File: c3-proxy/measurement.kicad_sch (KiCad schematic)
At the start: 31 parts, among them Q8 DMP2035UQ-7, SW2 SW_DP3T, U1 MCP2221AxST, U5 TS5A21366, U6 MAX892LEUA+T, U7 MIC23050-SYML, U8 LTC4412xS6

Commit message: layout cleanup, add bypass to U1-Vdd
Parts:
- added C10: 100n, oresat-passives:0603-C-NOSILK, symbol Device:C_Small
- D1, D2, D3, D4: footprint oresat-passives:0603-C-NOSILK -> LED_SMD:LED_0603_1608Metric
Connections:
- net 3.3V: now also C10.2
- net GND: now also C10.1
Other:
- note added: "Bypass for pin 1"

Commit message: polishing, adding 3D paths
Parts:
- C10: DPN 490-GRT188R71E105KE13DCT-ND -> 399-6856-1-ND; MFR Murata Electronics -> KEMET; MPN GRT188R71E105KE13D -> C0603C104K5RACAUTO
- R13, R14: DPN RMCF0603FT10K0CT-ND -> RMCF0603FT4K70CT-ND; MPN RMCF0603FT10K0 -> RMCF0603FT4K70
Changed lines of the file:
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@@
 			)
 		)
-		(property "Description" "10 kOhms ±1% 0.1W, 1/10W Chip Resistor 0603 (1608 Metric) Automotive AEC-Q200 Thick Film"
+		(property "Description" "4.7 kOhms ±1% 0.1W, 1/10W Chip Resistor 0603 (1608 Metric) Automotive AEC-Q200 Thick Film"
 			(at 181.61 140.97 0)
 			(hide yes)
@@
 			)
 		)
-		(property "DPN" "RMCF0603FT10K0CT-ND"
+		(property "DPN" "RMCF0603FT4K70CT-ND"
 			(at 181.61 140.97 0)
 			(hide yes)
@@
 			)
 		)
-		(property "MPN" "RMCF0603FT10K0"
+		(property "MPN" "RMCF0603FT4K70"
 			(at 181.61 140.97 0)
 			(hide yes)
@@
 			)
 		)
-		(property "Description" "10 kOhms ±1% 0.1W, 1/10W Chip Resistor 0603 (1608 Metric) Automotive AEC-Q200 Thick Film"
+		(property "Description" "4.7 kOhms ±1% 0.1W, 1/10W Chip Resistor 0603 (1608 Metric) Automotive AEC-Q200 Thick Film"
 			(at 186.69 140.97 0)
 			(hide yes)
@@
 			)
 		)
-		(property "DPN" "RMCF0603FT10K0CT-ND"
+		(property "DPN" "RMCF0603FT4K70CT-ND"
 			(at 186.69 140.97 0)
 			(hide yes)
@@
 			)
 		)
-		(property "MPN" "RMCF0603FT10K0"
+		(property "MPN" "RMCF0603FT4K70"
 			(at 186.69 140.97 0)
 			(hide yes)
@@
 			)
 		)
-		(property "Datasheet" "https://search.murata.co.jp/Ceramy/image/img/A01X/G101/ENG/GRT188R71E105KE13-01.pdf"
+		(property "Datasheet" "https://search.kemet.com/download/specsheet/C0603C104K5RACAUTO"
 			(at 129.54 143.51 0)
 			(hide yes)
@@
 			)
 		)
-		(property "Description" "1 µF ±10% 25V Ceramic Capacitor X7R 0603 (1608 Metric)"
+		(property "Description" "0.1 µF ±10% 50V Ceramic Capacitor X7R 0603 (1608 Metric)"
 			(at 129.54 133.35 0)
 			(hide yes)
@@
 			)
 		)
-		(property "DPN" "490-GRT188R71E105KE13DCT-ND"
+		(property "DPN" "399-6856-1-ND"
 			(at 129.54 143.51 0)
 			(hide yes)
@@
 			)
 		)
-		(property "MFR" "Murata Electronics"
+		(property "MFR" "KEMET"
 			(at 129.54 143.51 0)
 			(hide yes)
@@
 			)
 		)
-		(property "MPN" "GRT188R71E105KE13D"
+		(property "MPN" "C0603C104K5RACAUTO"
 			(at 129.54 143.51 0)
 			(hide yes)

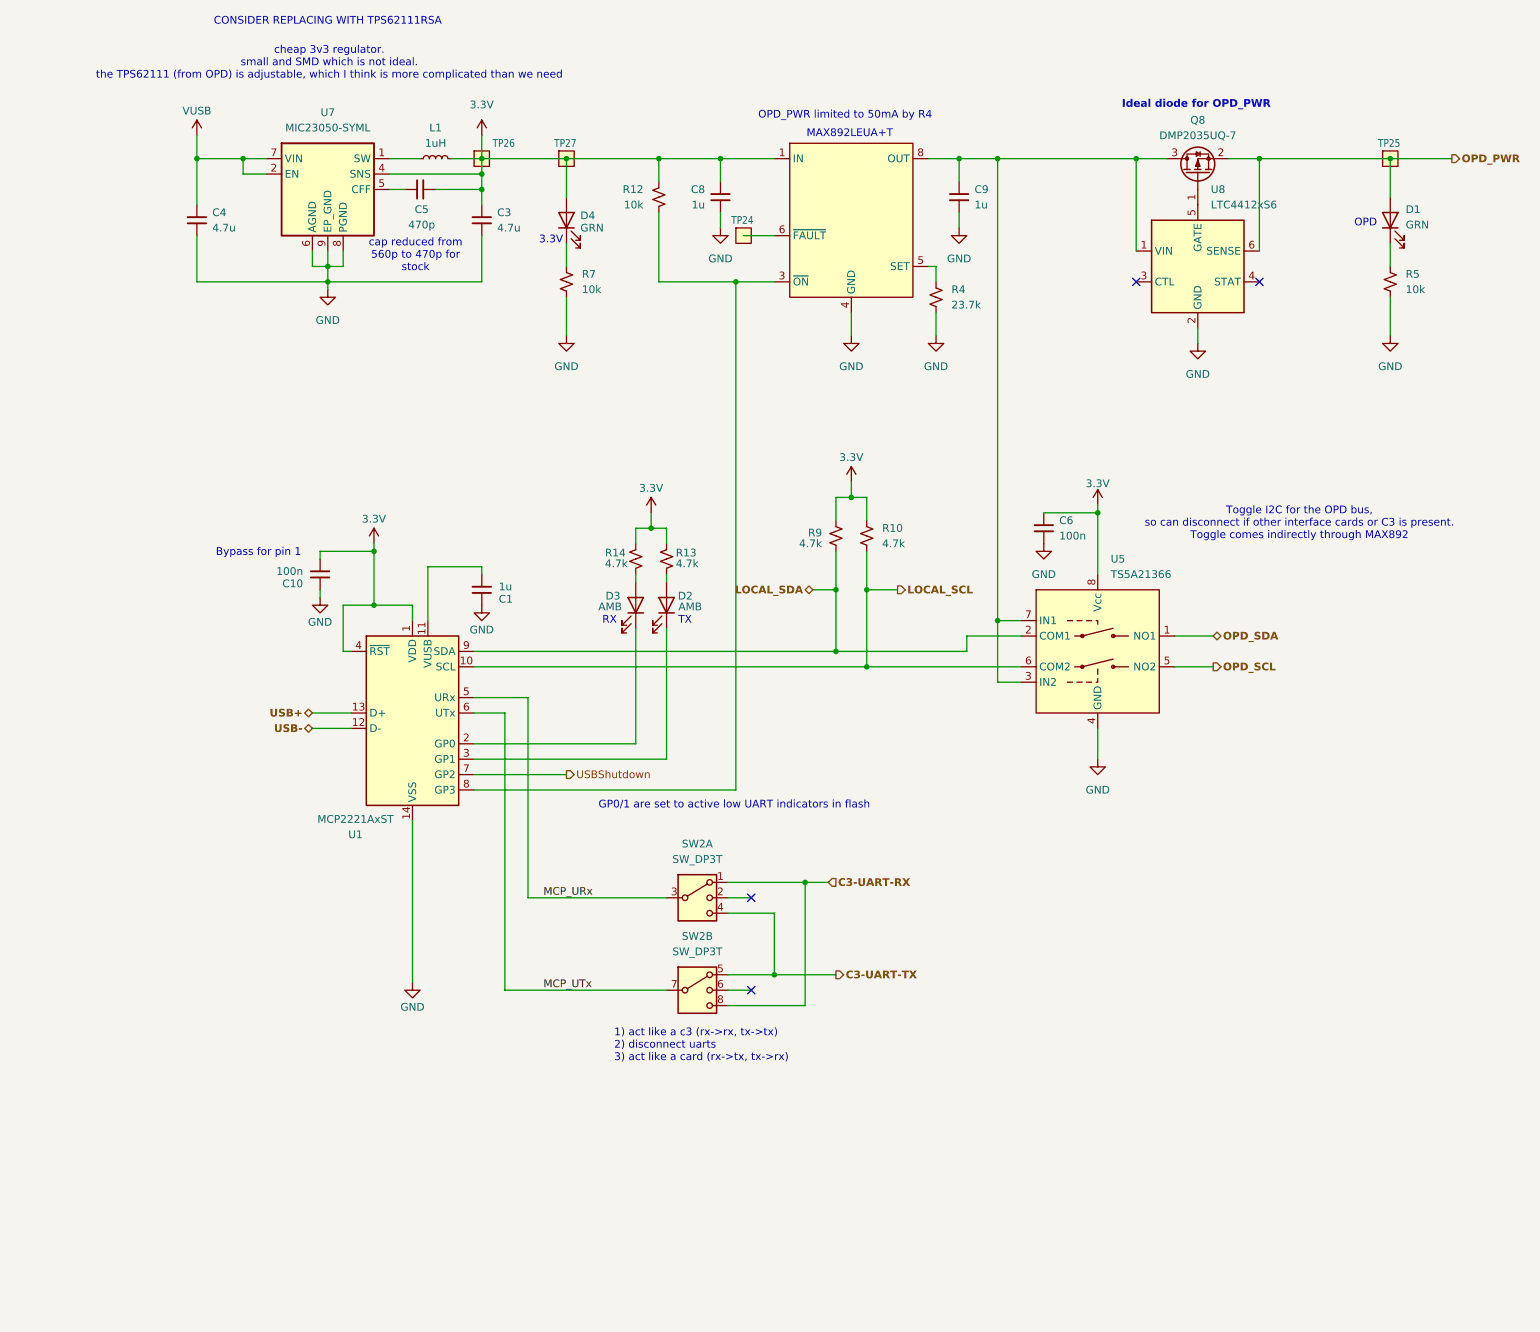
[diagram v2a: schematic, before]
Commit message: Final tweaks on v1.1.
Added more LEDs for main power, polished high power connections, DRC, ERC, etc. Added release folder.
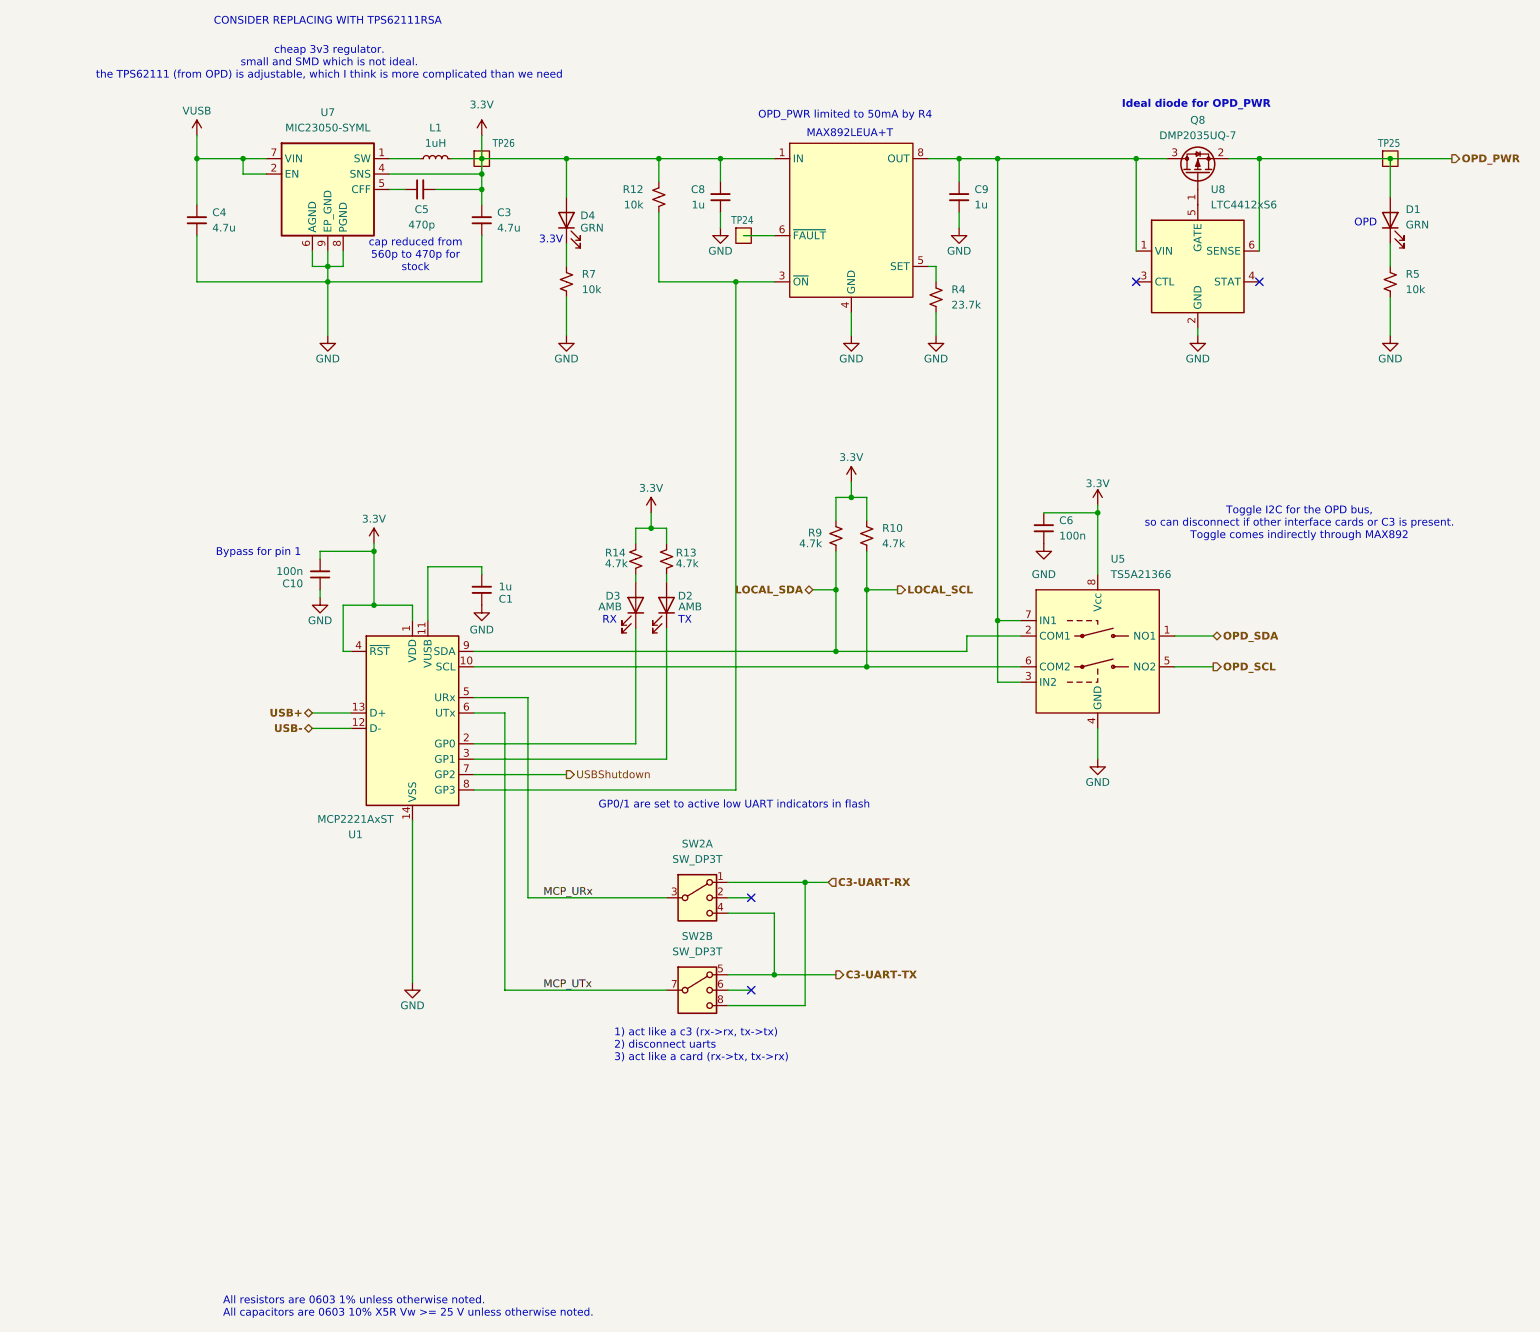
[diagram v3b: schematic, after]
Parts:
- removed TP27: Test-Point, oresat-misc:TestPoint-0.75mm-th, symbol oresat-misc:Test-Point-0.75mm-th
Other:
- note added: "All resistors are 0603 1% unless otherwise noted. All capacitors are 0603 10% X5R Vw >= 25 V unless otherwise noted."
- title: c3-Proxy card -> c3-Proxy Board
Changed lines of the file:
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@@
 	(paper "B")
 	(title_block
-		(title "c3-Proxy card")
-		(date "2026-09-07")
-		(rev "${REVISION}")
+		(title "c3-Proxy Board")
+		(date "2026-09-08")
+		(rev "1.1")
 		(company "Portland State Aerospace Society")
 	)
@@
 		)
 	)
+	(text "All resistors are 0603 1% unless otherwise noted.\nAll capacitors are 0603 10% X5R Vw >= 25 V unless otherwise noted."
+		(exclude_from_sim no)
+		(at 113.538 264.414 0)
+		(effects
+			(font
+				(size 1.27 1.27)
+			)
+			(justify left)
+		)
+	)
 	(text "Bypass for pin 1"
 		(exclude_from_sim no)
@@
 	(wire
 		(pts
-			(xy 274.32 102.87) (xy 274.32 105.41)
+			(xy 274.32 102.87) (xy 274.32 104.14)
 		)
 		(stroke
@@
 	(wire
 		(pts
-			(xy 130.81 95.25) (xy 130.81 96.52)
+			(xy 130.81 95.25) (xy 130.81 104.14)
 		)
 		(stroke
@@
 	)
 	(symbol
-		(lib_id "oresat-misc:Test-Point-0.75mm-th")
-		(at 170.18 74.93 0)
-		(unit 1)
-		(body_style 1)
-		(exclude_from_sim yes)
-		(in_bom no)
-		(on_board yes)
-		(in_pos_files yes)
-		(dnp no)
-		(property "Reference" "TP27"
-			(at 168.148 72.39 0)
-			(show_name no)
-			(do_not_autoplace no)
-			(effects
-				(font
-					(size 1.27 1.0795)
-				)
-				(justify left)
-			)
-		)
-		(property "Value" "Test-Point"
-			(at 170.18 67.31 0)
-			(hide yes)
-			(show_name no)
-			(do_not_autoplace no)
-			(effects
-				(font
-					(size 1.27 1.27)
-				)
-			)
-		)
-		(property "Footprint" "oresat-misc:TestPoint-0.75mm-th"
-			(at 170.18 64.77 0)
-			(hide yes)
-			(show_name no)
-			(do_not_autoplace no)
-			(effects
-				(font
-					(size 1.27 1.27)
-				)
-			)
-		)
-		(property "Datasheet" ""
-			(at 170.18 74.93 0)
-			(hide yes)
-			(show_name no)
-			(do_not_autoplace no)
-			(effects
-				(font
-					(size 1.27 1.27)
-				)
-			)
-		)
-		(property "Description" "0.75 mm TH test point; good for scope probes and jumpers"
-			(at 170.18 74.93 0)
-			(hide yes)
-			(show_name no)
-			(do_not_autoplace no)
-			(effects
-				(font
-					(size 1.27 1.27)
-				)
-			)
-		)
-		(pin "1"
-		)
-		(instances
-			(project "c3-proxy"
-				(path "/1a9202c4-e698-4c93-952c-ee3e64e9e49c/ad201ad7-0b68-497a-9bd5-92d5158f3b08"
-					(reference "TP27")
-					(unit 1)
-				)
-			)
-		)
-	)
-	(symbol
 		(lib_id "Regulator_Switching:MIC23050-SYML")
 		(at 130.81 80.01 0)
@@
 		)
 		(property "Value" "GND"
-			(at 144.78 214.884 0)
+			(at 144.78 214.63 0)
 			(show_name no)
 			(do_not_autoplace no)
@@
 		(in_pos_files yes)
 		(dnp no)
-		(fields_autoplaced yes)
 		(property "Reference" "#PWR011"
 			(at 257.81 180.34 0)
@@
 		)
 		(property "Value" "GND"
-			(at 257.81 179.07 0)
+			(at 257.81 177.8 0)
 			(show_name no)
 			(do_not_autoplace no)
@@
 		(in_pos_files yes)
 		(dnp no)
-		(fields_autoplaced yes)
 		(property "Reference" "#PWR017"
 			(at 306.07 110.49 0)
@@
 		)
 		(property "Value" "GND"
-			(at 306.07 109.22 0)
+			(at 306.07 107.95 0)
 			(show_name no)
 			(do_not_autoplace no)
@@
 	(symbol
 		(lib_id "power:GND")
-		(at 274.32 105.41 0)
+		(at 274.32 104.14 0)
 		(unit 1)
 		(body_style 1)
@@
 		(in_pos_files yes)
 		(dnp no)
-		(fields_autoplaced yes)
 		(property "Reference" "#PWR016"
-			(at 274.32 111.76 0)
+			(at 274.32 110.49 0)
 			(hide yes)
 			(show_name no)
@@
 		)
 		(property "Value" "GND"
-			(at 274.32 110.49 0)
+			(at 274.32 107.95 0)
 			(show_name no)
 			(do_not_autoplace no)
@@
 		)
 		(property "Footprint" ""
-			(at 274.32 105.41 0)
+			(at 274.32 104.14 0)
 			(hide yes)
 			(show_name no)
@@
 		)
 		(property "Datasheet" ""
-			(at 274.32 105.41 0)
+			(at 274.32 104.14 0)
 			(hide yes)
 			(show_name no)
@@
 		)
 		(property "Description" "Power symbol creates a global label with name \"GND\" , ground"
-			(at 274.32 105.41 0)
+			(at 274.32 104.14 0)
 			(hide yes)
 			(show_name no)
@@
 		)
 		(property "Value" "GND"
-			(at 129.54 151.384 0)
+			(at 129.54 151.13 0)
 			(show_name no)
 			(do_not_autoplace no)
@@
 		(in_pos_files yes)
 		(dnp no)
-		(fields_autoplaced yes)
 		(property "Reference" "#PWR026"
 			(at 234.95 92.71 0)
@@
 		)
 		(property "Value" "GND"
-			(at 234.95 91.44 0)
+			(at 234.95 90.17 0)
 			(show_name no)
 			(do_not_autoplace no)
@@
 	(symbol
 		(lib_id "power:GND")
-		(at 130.81 96.52 0)
+		(at 130.81 104.14 0)
 		(unit 1)
 		(body_style 1)
@@
 		(in_pos_files yes)
 		(dnp no)
-		(fields_autoplaced yes)
 		(property "Reference" "#PWR015"
-			(at 130.81 102.87 0)
+			(at 130.81 110.49 0)
 			(hide yes)
 			(show_name no)
@@
 		)
 		(property "Value" "GND"
-			(at 130.81 101.6 0)
+			(at 130.81 107.95 0)
 			(show_name no)
 			(do_not_autoplace no)
@@
 		)
 		(property "Footprint" ""
-			(at 130.81 96.52 0)
+			(at 130.81 104.14 0)
 			(hide yes)
 			(show_name no)
@@
 		)
 		(property "Datasheet" ""
-			(at 130.81 96.52 0)
+			(at 130.81 104.14 0)
 			(hide yes)
 			(show_name no)
@@
 		)
 		(property "Description" "Power symbol creates a global label with name \"GND\" , ground"
-			(at 130.81 96.52 0)
+			(at 130.81 104.14 0)
 			(hide yes)
 			(show_name no)
@@
 		(in_pos_files yes)
 		(dnp no)
-		(fields_autoplaced yes)
 		(property "Reference" "#PWR014"
 			(at 217.17 110.49 0)
@@
 		)
 		(property "Value" "GND"
-			(at 217.17 109.22 0)
+			(at 217.17 107.95 0)
 			(show_name no)
 			(do_not_autoplace no)
@@
 		(in_pos_files yes)
 		(dnp no)
-		(fields_autoplaced yes)
 		(property "Reference" "#PWR027"
 			(at 170.18 110.49 0)
@@
 		)
 		(property "Value" "GND"
-			(at 170.18 109.22 0)
+			(at 170.18 107.95 0)
 			(show_name no)
 			(do_not_autoplace no)
@@
 		(in_pos_files yes)
 		(dnp no)
-		(fields_autoplaced yes)
 		(property "Reference" "#PWR025"
 			(at 195.58 92.71 0)
@@
 		)
 		(property "Value" "GND"
-			(at 195.58 91.44 0)
+			(at 195.58 90.17 0)
 			(show_name no)
 			(do_not_autoplace no)
@@
 		(in_pos_files yes)
 		(dnp no)
-		(fields_autoplaced yes)
 		(property "Reference" "#PWR013"
 			(at 231.14 110.49 0)
@@
 		)
 		(property "Value" "GND"
-			(at 231.14 109.22 0)
+			(at 231.14 107.95 0)
 			(show_name no)
 			(do_not_autoplace no)
